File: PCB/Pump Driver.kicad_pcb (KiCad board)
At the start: 2 copper layers, 44 parts, among them P1 CONN_13X2, P10 CONN_2, P11 CONN_2, P12 CONN_2, P2 CONN_9, P3 CONN_2, P4 CONN_2, P5 CONN_2, P6 CONN_2, P7 CONN_2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

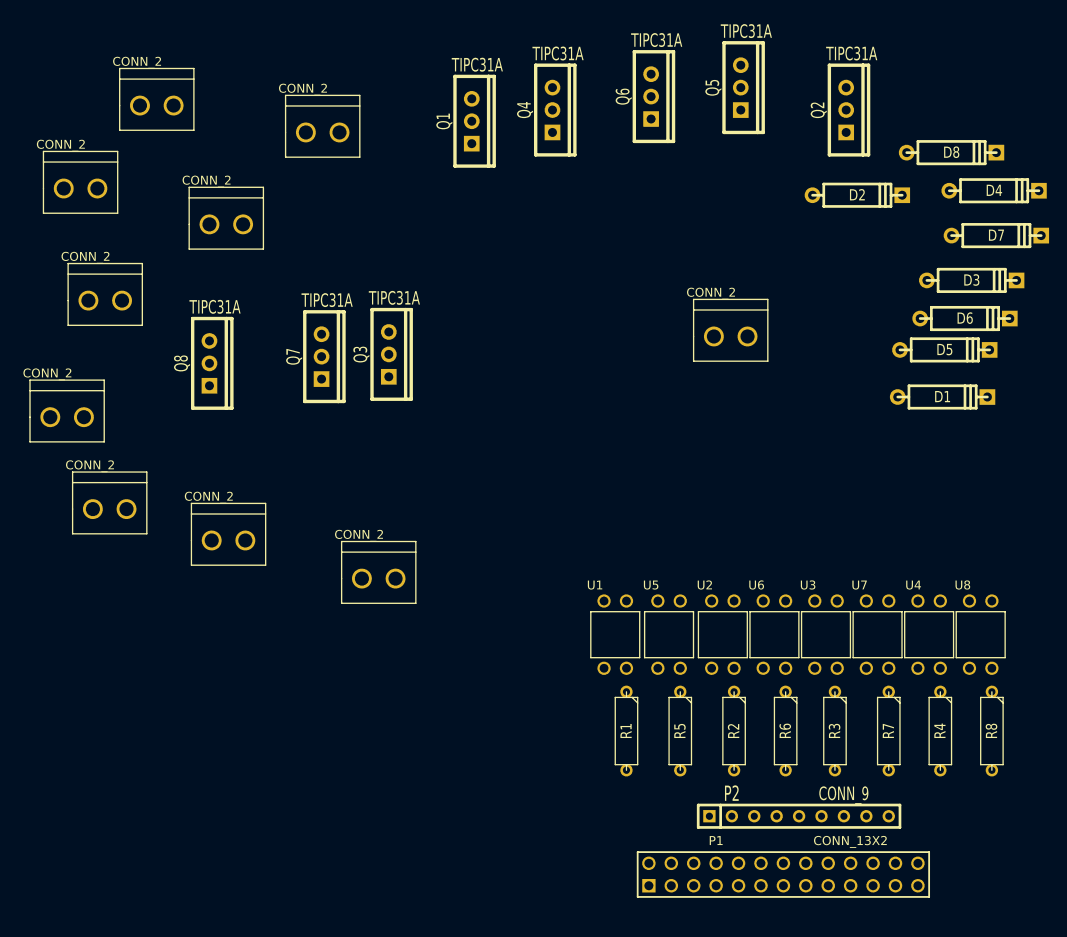
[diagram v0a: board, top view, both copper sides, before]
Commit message: Lay all tracks & ground plane. Correct schematic
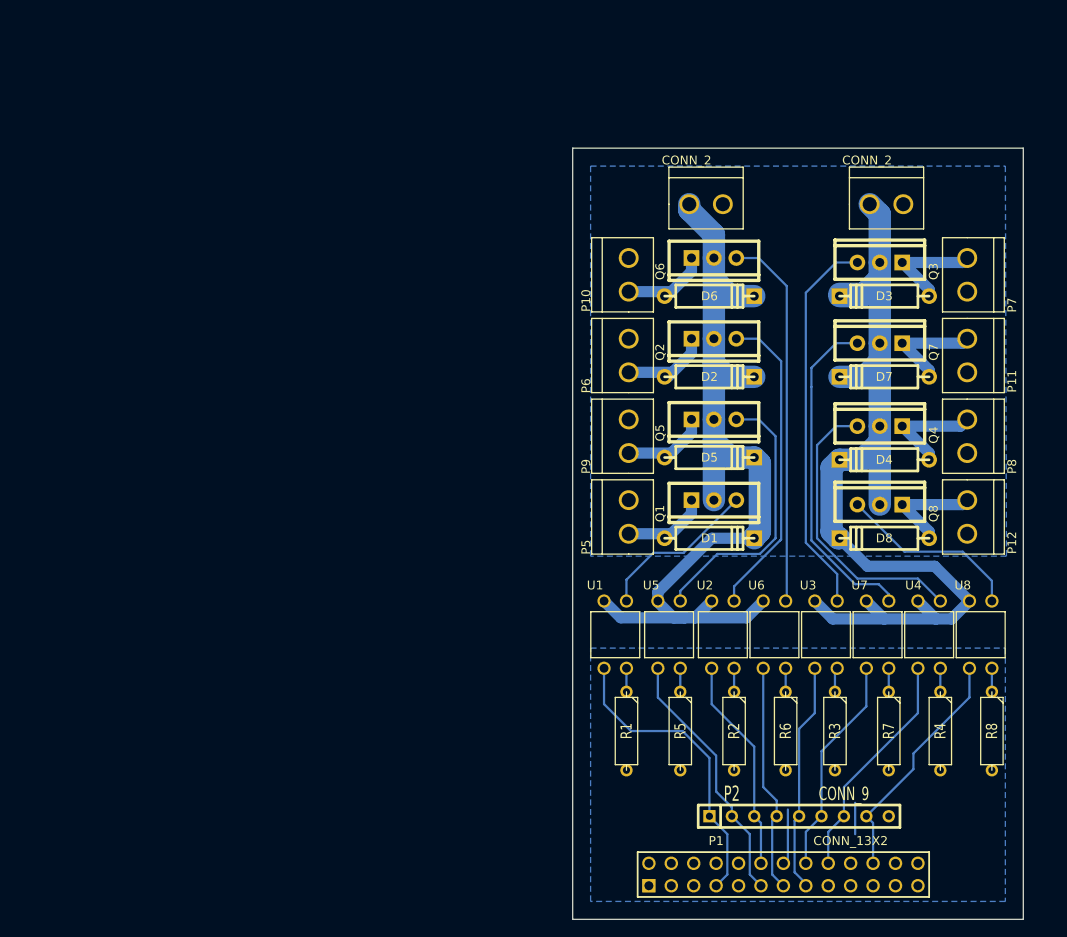
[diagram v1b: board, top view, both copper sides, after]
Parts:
- moved P8 99.6 mm to (152.9, 62.0), turned to 270 degrees
- moved P4 91.3 mm to (141.9, 37.6)
- moved P12 85.7 mm to (152.9, 71.1), turned to 270 degrees
- moved Q8 77.6 mm to (143.0, 71.6), turned to 90 degrees
- moved P7 76.3 mm to (152.9, 43.7), turned to 270 degrees
- moved P9 65.7 mm to (114.6, 65.8), turned to 90 degrees
- moved Q7 63.3 mm to (143.0, 53.3), turned to 90 degrees
- moved P3 63.2 mm to (121.4, 37.6)
- moved P6 61.8 mm to (114.6, 56.6), turned to 90 degrees
- moved Q3 56.6 mm to (143.0, 44.2), turned to 90 degrees
- moved Q4 51.6 mm to (143.0, 62.7), turned to 90 degrees
- moved Q1 50.9 mm to (124.2, 71.1), turned to 270 degrees
- moved P10 48.1 mm to (114.6, 47.5), turned to 90 degrees
- moved D8 44.3 mm to (143.5, 75.4), turned to 180 degrees
- moved Q5 37.7 mm to (124.2, 62.0), turned to 270 degrees
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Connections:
- D3 pad 2: +12P -> +12V
- D4 pad 2: +12P -> +12V
- D7 pad 2: +12P -> +12V
- D8 pad 2: +12P -> +12V
- P4 pad 1: (no net) -> +12V
- Q3 pad 3: +12P -> +12V
- Q4 pad 3: +12P -> +12V
- Q7 pad 3: +12P -> +12V
- Q8 pad 3: +12P -> +12V
- U3 pad 4: +12P -> +12V
- U4 pad 4: +12P -> +12V
- U7 pad 4: +12P -> +12V
- U8 pad 4: +12P -> +12V
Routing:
- net +12V: track 0.00 -> 108.3 mm, vias 0 -> 1
- net +12P: track 0.00 -> 101.0 mm
- net N-0000028: track 0.00 -> 43.7 mm
- net N-0000042: track 0.00 -> 42.8 mm
- net N-000005: track 0.00 -> 38.0 mm
- net N-0000022: track 0.00 -> 35.5 mm
- net IO1: track 0.00 -> 34.4 mm
- net N-0000026: track 0.00 -> 32.9 mm
- net N-0000024: track 0.00 -> 31.2 mm
- net IO2: track 0.00 -> 29.5 mm
- net IO8: track 0.00 -> 27.3 mm
- net IO7: track 0.00 -> 26.3 mm
- net IO5: track 0.00 -> 26.1 mm
- net IO4: track 0.00 -> 26.0 mm
- net N-0000027: track 0.00 -> 25.2 mm
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- added copper zone on B.Cu, net GND
- added copper zone on B.Cu, net GNDPWR
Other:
- board outline added: 51.1 x 87.4 mm
- net class Power added: clearance 0.254, trace_width 2.54, via_dia 0.889, via_drill 0.635
